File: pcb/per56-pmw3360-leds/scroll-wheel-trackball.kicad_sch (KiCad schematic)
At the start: 20 parts, among them IC1 AP7335-WG-7, SW1 RotaryEncoder, U1 PMW3360DM-T2QU, U2 TXS0104EDR

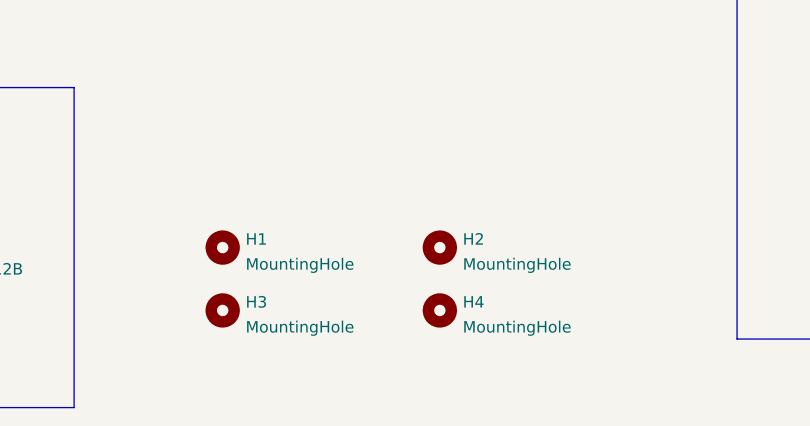
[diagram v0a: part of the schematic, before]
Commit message: added module mounting footprints to make designing both the module pcbs and the keyboard pcbs mounting for modules easier
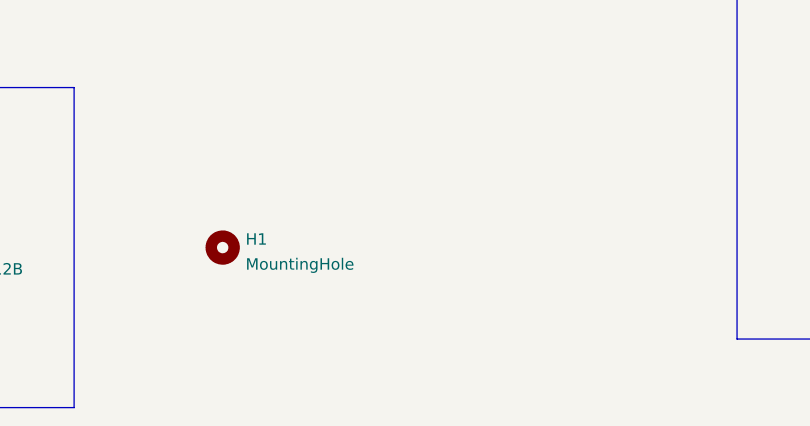
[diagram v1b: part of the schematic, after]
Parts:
- removed H2, H3, H4: MountingHole, MountingHole:MountingHole_2.2mm_M2_Pad, symbol Mechanical:MountingHole
- H1: footprint MountingHole:MountingHole_2.2mm_M2_Pad -> vik:vik-module-mounting-large
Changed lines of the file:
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@@
-    )
-  )
-  (symbol (lib_id "Mechanical:MountingHole") (at 179.07 182.88 0) (unit 1)
-    (in_bom yes) (on_board yes) (dnp no) (fields_autoplaced)
-    (property "Reference" "H2" (at 181.61 181.9715 0)
-      (effects (font (size 1.27 1.27)) (justify left))
-    )
-    (property "Value" "MountingHole" (at 181.61 184.7466 0)
-      (effects (font (size 1.27 1.27)) (justify left))
-    )
-    (property "Footprint" "MountingHole:MountingHole_2.2mm_M2_Pad" (at 179.07 182.88 0)
-      (effects (font (size 1.27 1.27)) hide)
-    )
-    (property "Datasheet" "~" (at 179.07 182.88 0)
-      (effects (font (size 1.27 1.27)) hide)
-    )
-    (instances
-      (project "scroll-wheel-trackball"
-        (path "/61fe293f-6808-4b7f-9340-9aaac7054a97"
-          (reference "H2") (unit 1)
-        )
-      )
     )
   )
@@
         (path "/61fe293f-6808-4b7f-9340-9aaac7054a97"
           (reference "#PWR0108") (unit 1)
-        )
-      )
-    )
-  )
-  (symbol (lib_id "Mechanical:MountingHole") (at 179.07 189.865 0) (unit 1)
-    (in_bom yes) (on_board yes) (dnp no) (fields_autoplaced)
-    (property "Reference" "H4" (at 181.61 188.9565 0)
-      (effects (font (size 1.27 1.27)) (justify left))
-    )
-    (property "Value" "MountingHole" (at 181.61 191.7316 0)
-      (effects (font (size 1.27 1.27)) (justify left))
-    )
-    (property "Footprint" "MountingHole:MountingHole_2.2mm_M2_Pad" (at 179.07 189.865 0)
-      (effects (font (size 1.27 1.27)) hide)
-    )
-    (property "Datasheet" "~" (at 179.07 189.865 0)
-      (effects (font (size 1.27 1.27)) hide)
-    )
-    (instances
-      (project "scroll-wheel-trackball"
-        (path "/61fe293f-6808-4b7f-9340-9aaac7054a97"
-          (reference "H4") (unit 1)
         )
       )
@@
       (effects (font (size 1.27 1.27)) (justify left))
     )
-    (property "Footprint" "MountingHole:MountingHole_2.2mm_M2_Pad" (at 154.94 182.88 0)
+    (property "Footprint" "vik:vik-module-mounting-large" (at 154.94 182.88 0)
       (effects (font (size 1.27 1.27)) hide)
     )
@@
         )
       )
-    )
-  )
-  (symbol (lib_id "Mechanical:MountingHole") (at 154.94 189.865 0) (unit 1)
-    (in_bom yes) (on_board yes) (dnp no) (fields_autoplaced)
-    (property "Reference" "H3" (at 157.48 188.9565 0)
-      (effects (font (size 1.27 1.27)) (justify left))
-    )
-    (property "Value" "MountingHole" (at 157.48 191.7316 0)
-      (effects (font (size 1.27 1.27)) (justify left))
-    )
-    (property "Footprint" "MountingHole:MountingHole_2.2mm_M2_Pad" (at 154.94 189.865 0)
-      (effects (font (size 1.27 1.27)) hide)
-    )
-    (property "Datasheet" "~" (at 154.94 189.865 0)
-      (effects (font (size 1.27 1.27)) hide)
-    )
-    (instances
-      (project "scroll-wheel-trackball"
-        (path "/61fe293f-6808-4b7f-9340-9aaac7054a97"
-          (reference "H3") (unit 1)
-        )
-      )
